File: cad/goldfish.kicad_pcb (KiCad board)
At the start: 2 copper layers, 17.8 x 33 mm, 27 parts, among them J1 USB_C_Receptacle_USB2.0, J2 Conn_01x02, J3 Conn_01x12, J4 Conn_01x12, J5 Conn_01x05, U1 ATmega32U4-M, U2 USBLC6-2P6, X1 16MHz

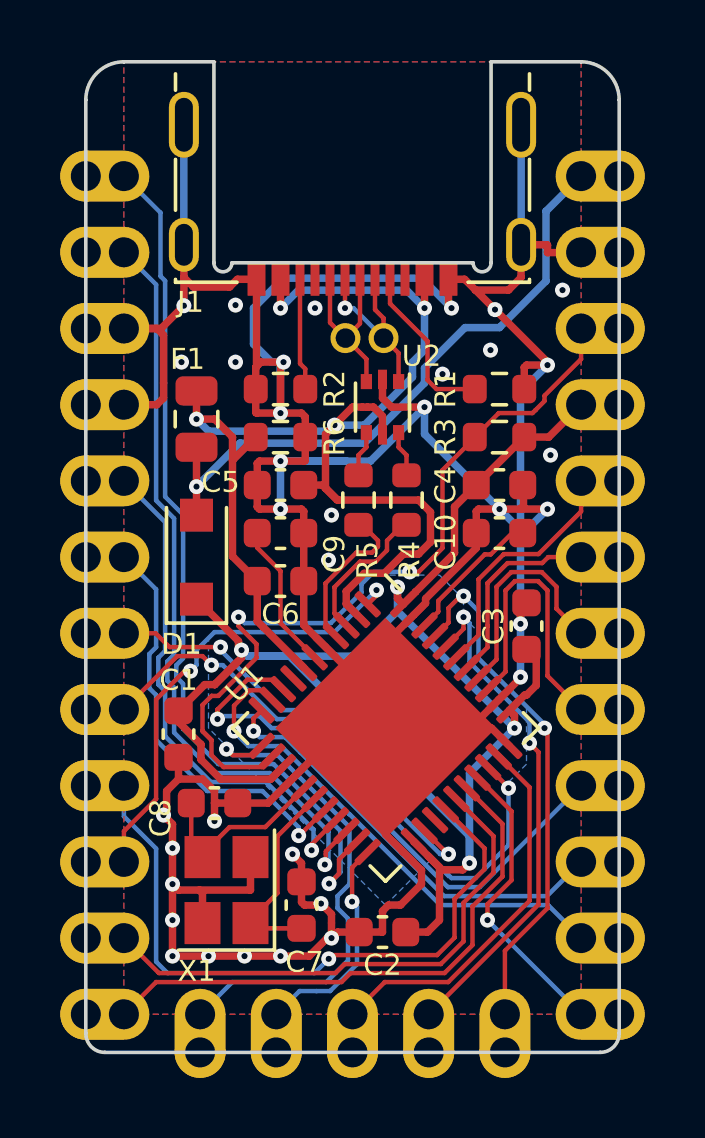
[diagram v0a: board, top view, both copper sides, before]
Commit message: corrected front silkscreens and added schematic PDF files
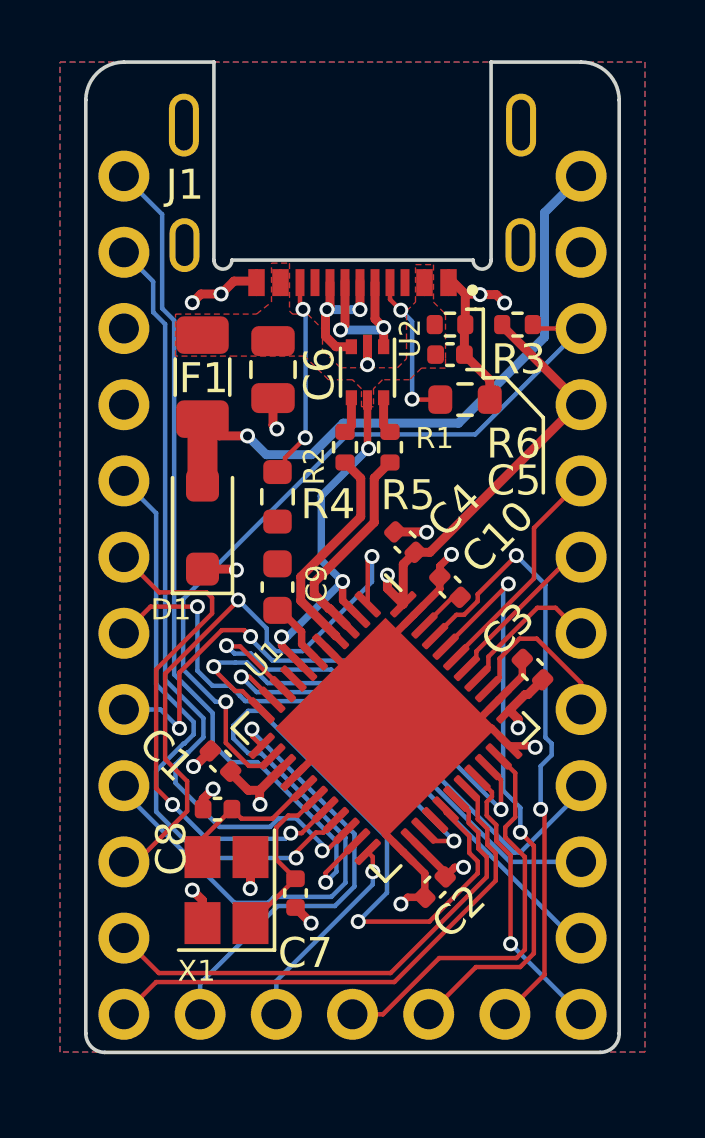
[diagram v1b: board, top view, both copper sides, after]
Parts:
- removed J2: Conn_01x02, Goldfish Pins:Pins_USB
- C1, C10, C2, C3, C4, C5: value 0u1 -> 100nF; footprint Capacitor_SMD:C_0603_1608Metric -> Capacitor_SMD:C_0402_1005Metric
- C6: value 4u7 -> 4.7uF; footprint Capacitor_SMD:C_0603_1608Metric -> Capacitor_SMD:C_0805_2012Metric
- C7, C8: value 22p -> 15pF; footprint Capacitor_SMD:C_0603_1608Metric -> Capacitor_SMD:C_0402_1005Metric
- C9: value 1u -> 1uF
- F1: footprint Fuse:Fuse_0805_2012Metric -> Fuse:Fuse_1206_3216Metric
- J1: value USB_C_Receptacle_USB2.0 -> USB_C_Receptacle_16P; footprint Molex 216990_GCT USB45xx_HRO TYPE-C-31-M-13x:Molex-216990_GCT-USB45xx_HRO-TYPE-C-31-M-13x -> Goldfish_V2:TYPE-610-1.6-T3
- J3, J4: footprint Goldfish Pins:Pins_x12_Castellated -> Goldfish_V2:Pins_x12
- J5: footprint Goldfish Pins:Pins_x05_Castellated -> Goldfish_V2:Pins_x05
- R3, R6: footprint Resistor_SMD:R_0603_1608Metric -> Resistor_SMD:R_0402_1005Metric
- R4, R5: value 22 -> 22R; footprint Resistor_SMD:R_0603_1608Metric -> Resistor_SMD:R_0402_1005Metric
- U1: value ATmega32U4-M -> ATmega32U4-MU
- moved C5 7.13 mm to (33.2, 33.2), turned to 0 degrees
- moved C6 7.05 mm to (27.4, 33.8), turned to -90 degrees
- moved R6 6.78 mm to (33.2, 32.2)
- moved R3 3.80 mm to (35.5, 32.2), turned to 180 degrees
- moved C4 3.68 mm to (31.8, 39.5), turned to 135 degrees
- moved R2 3.59 mm to (27.5, 38.0), turned to 90 degrees
- moved C10 2.44 mm to (33.2, 41.0), turned to 135 degrees
- moved C2 2.30 mm to (32.8, 51.0), turned to -135 degrees
- moved J1 2.11 mm to (30.0, 25.6)
- moved R5 1.85 mm to (31.2, 36.3)
- moved R4 1.82 mm to (29.8, 36.3)
- moved C9 1.80 mm to (27.5, 41.0), turned to 90 degrees
- moved C1 1.66 mm to (25.6, 46.8), turned to 135 degrees
- moved C3 1.46 mm to (36.0, 43.8), turned to 135 degrees
- moved F1 1.41 mm to (25.0, 34.0)
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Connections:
- net /RESET renamed /~{RESET}
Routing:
- net GND: track 160.1 -> 48.0 mm, vias 35 -> 15
- net VCC: track 59.2 -> 23.0 mm, vias 4 -> 5
- net VBUS: track 45.4 -> 12.6 mm, vias 4 -> 3
- net /PD7: track 22.1 -> 33.9 mm
- net /PE6: track 15.6 -> 20.0 mm
- net /PF7: track 9.62 -> 5.66 mm
- net Net-(U1-AREF): track 4.76 -> 1.58 mm
- net /PD0: track 14.2 -> 17.4 mm, vias 1 -> 2
- net /PF1: track 17.0 -> 20.1 mm
- net /PF0: track 17.5 -> 20.5 mm
- net Net-(J1-CC2): track 3.73 -> 6.74 mm, vias 0 -> 2
- net /PB3: track 14.5 -> 17.4 mm
- net Net-(U1-UCAP): track 4.93 -> 2.28 mm
- net /PF6: track 7.61 -> 4.99 mm
- net /PD1: track 17.6 -> 19.8 mm
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- added copper zone on In1.Cu, net GND
- added copper zone on F.Cu, net VBUS
- added copper zone on In2.Cu, net VCC
- removed copper zone on B.Cu, net VCC
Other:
- outline, holes or cut-outs redrawn
- copper layers 2 -> 4
- board text added: "v2 rev1"
- board text removed: "v2 rev0"
